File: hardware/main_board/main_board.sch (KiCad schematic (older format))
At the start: 45 parts, among them P1 USB_OTG, P2 CONN_01X02, Q1 MMBT2222, Q2 MMBT2222, SW1 SW_DPDT_x2, SW2 SW_Push, U1 ESP-12E, U2 CP2104, U3 MCP9808, U4 MMA8451Q, U5 MCP73831/2, U6 AP2112

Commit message: Separating design into main and programmer boards
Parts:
- P1: symbol USB_OTG -> USB_OTG-RESCUE-main_board
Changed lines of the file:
@@
 EESchema Schematic File Version 2
+LIBS:main_board-rescue
 LIBS:power
 LIBS:device
@@
 LIBS:zetex
 LIBS:Zilog
-LIBS:wifi_hydrometer-cache
+LIBS:main_board-cache
 EELAYER 25 0
 EELAYER END
@@
 GPIO15
 $Comp
-L USB_OTG P1
+L USB_OTG-RESCUE-main_board P1
 U 1 1 58B960C2
 P 1200 2350
@@
 	1450 4100 1350 4200
 Wire Wire Line
-	1350 4400 1350 4200
+	1350 4200 1350 4400
 Wire Wire Line
 	900  4400 1450 4400
@@
 	1450 4000 1350 3900
 Wire Wire Line
-	1350 3700 1350 3900
+	1350 3900 1350 3700
 Wire Wire Line
 	900  3700 1450 3700

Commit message: Moved components to programmer board
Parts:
- removed C1, C9: 1u, Capacitors_SMD:C_0603, symbol C
- removed P1: USB_OTG, footprint:10118192, symbol USB_OTG-RESCUE-main_board
- removed Q1, Q2: MMBT2222, TO_SOT_Packages_SMD:SOT-23, symbol Q_NPN_BEC
- removed R10, R11, R18, R19, R20, R7: 10k, Resistors_SMD:R_0603, symbol R
- removed U2: CP2104, Housings_DFN_QFN:QFN-24-1EP_4x4mm_Pitch0.5mm, symbol CP2104
- added J?: Conn_01x06, symbol Conn_01x06
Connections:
- net labels added: PROG_RXD, PROG_TXD
- net labels removed: DTR, RTS, RXD, TXD, USB_D+, USB_D-
- wire segments 148 -> 107
- no-connect marks 14 -> 10
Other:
- note added: "5V\nDETECT"
- note removed: "USB\nDETECT"
- moved on the sheet: C5, C6, C7, C8, D1, D3, D4, P2, R12, R13, SW1A, SW1B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

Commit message: Working on schematic
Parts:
- removed D4: MBR120, footprint:SOD-123FL, symbol D_Schottky
- removed J?: Conn_01x06, symbol Conn_01x06
- removed R1: 1k, Resistors_SMD:R_0603, symbol R_Small
- removed R2, R3: 10k, Resistors_SMD:R_0603, symbol R
- removed R6: 4.7k, Resistors_SMD:R_0603, symbol R
- removed SW2: SW_Push, footprint:KMR7, symbol SW_Push
- removed U1: ESP-12E, footprint:ESP-12E, symbol ESP-12E
- added C?: 1u, Capacitors_SMD:C_0603, symbol C
- added J?: eConn_02x03_Odd_Even, symbol Conn_02x03_Odd_Even
- added Q?: DMG3415U, TO_SOT_Packages_SMD:SOT-23, symbol Q_PMOS_GSD
- added R?: 100k, Resistors_SMD:R_0603, symbol R
- added U?: ESP-WROOM-32D, symbol ESP-WROOM-32D
- D1: value LED -> YLW
- D2: value LED -> RED
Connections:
- net labels added: 5V_SENSE, BAT_SENSE, LED, SCL, SDA
- net labels removed: ADC, CH_PD, GPIO12/MISO, GPIO13/MOSI, GPIO14/SCK, GPIO15, GPIO16, GPIO2, GPIO4/SDA, GPIO5/SCL
- wire segments 107 -> 98
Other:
- note removed: "5V\nDETECT"
- note removed: "BAT\nSENSE"
- moved on the sheet: C2, C3, C4, C5, C6, C7, C8, D1, D2, D3, P2, R12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

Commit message: Working on layout
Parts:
- removed C?: 1u, Capacitors_SMD:C_0603, symbol C
- removed R9: 47k, Resistors_SMD:R_0603, symbol R
- added C5, C9: 0.1u, Capacitors_SMD:C_0603, symbol C
- added C8: 10u, Capacitors_SMD:C_0805, symbol C
- added R7: 10k, Resistors_SMD:R_0603, symbol R
- D1: value YLW -> ORG
- J1: renamed from J?; footprint (none) -> Socket_Strips:Socket_Strip_Angled_2x03_Pitch2.54mm
- R8: value 24k -> 15k; Part 311-24.0KHRCT-ND -> 311-15.0KHRCT-ND
- U4: renamed from U?; footprint (none) -> footprint:ESP32-WROOM; Source (none) -> DigiKey
- gave numbers to parts that had none: 2
- renumbered C6 to C1, C2 to C10, C5 to C2, C7 to C3, C8 to C4, C3 to C6, C4 to C7, D3 to D2, D2 to D3, P2 to P1, R5 to R10, R14 to R11, R13 to R2, R16 to R3, R15 to R4, R17 to R5, R12 to R6, R4 to R9, U5 to U1, U6 to U2, U4 to U5
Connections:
- wire segments 98 -> 108
- no-connect marks 10 -> 21
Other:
- note added: "STRAPPING PINS:\nIO0\nIO2\nIO5\nIO12\nIO15"
- moved on the sheet: C10, R11

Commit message: Working on component placement
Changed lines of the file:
@@
 Connection ~ 8700 4700
-Wire Wire Line
-	1650 3900 1650 4100
 Wire Wire Line
 	3200 6650 3200 6000
@@
 NoConn ~ 6950 2400
 NoConn ~ 6950 2500
+Wire Wire Line
+	1650 3950 1650 4100
 $EndSCHEMATC

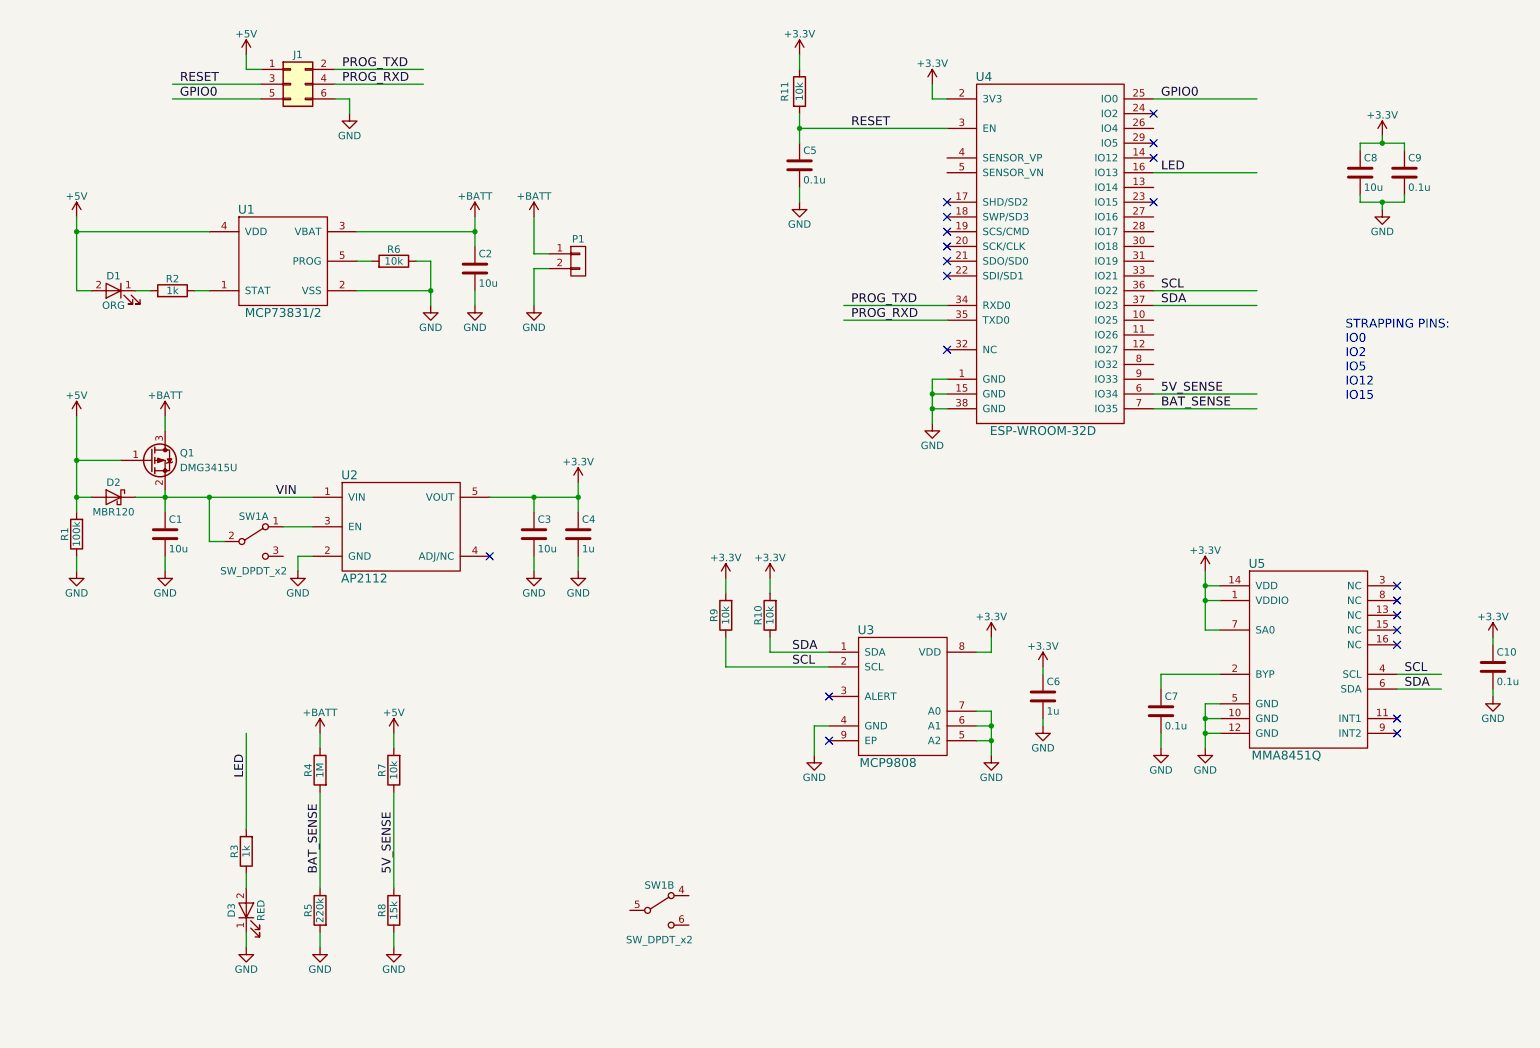
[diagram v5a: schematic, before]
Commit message: Added UV sensor.  Working on layout
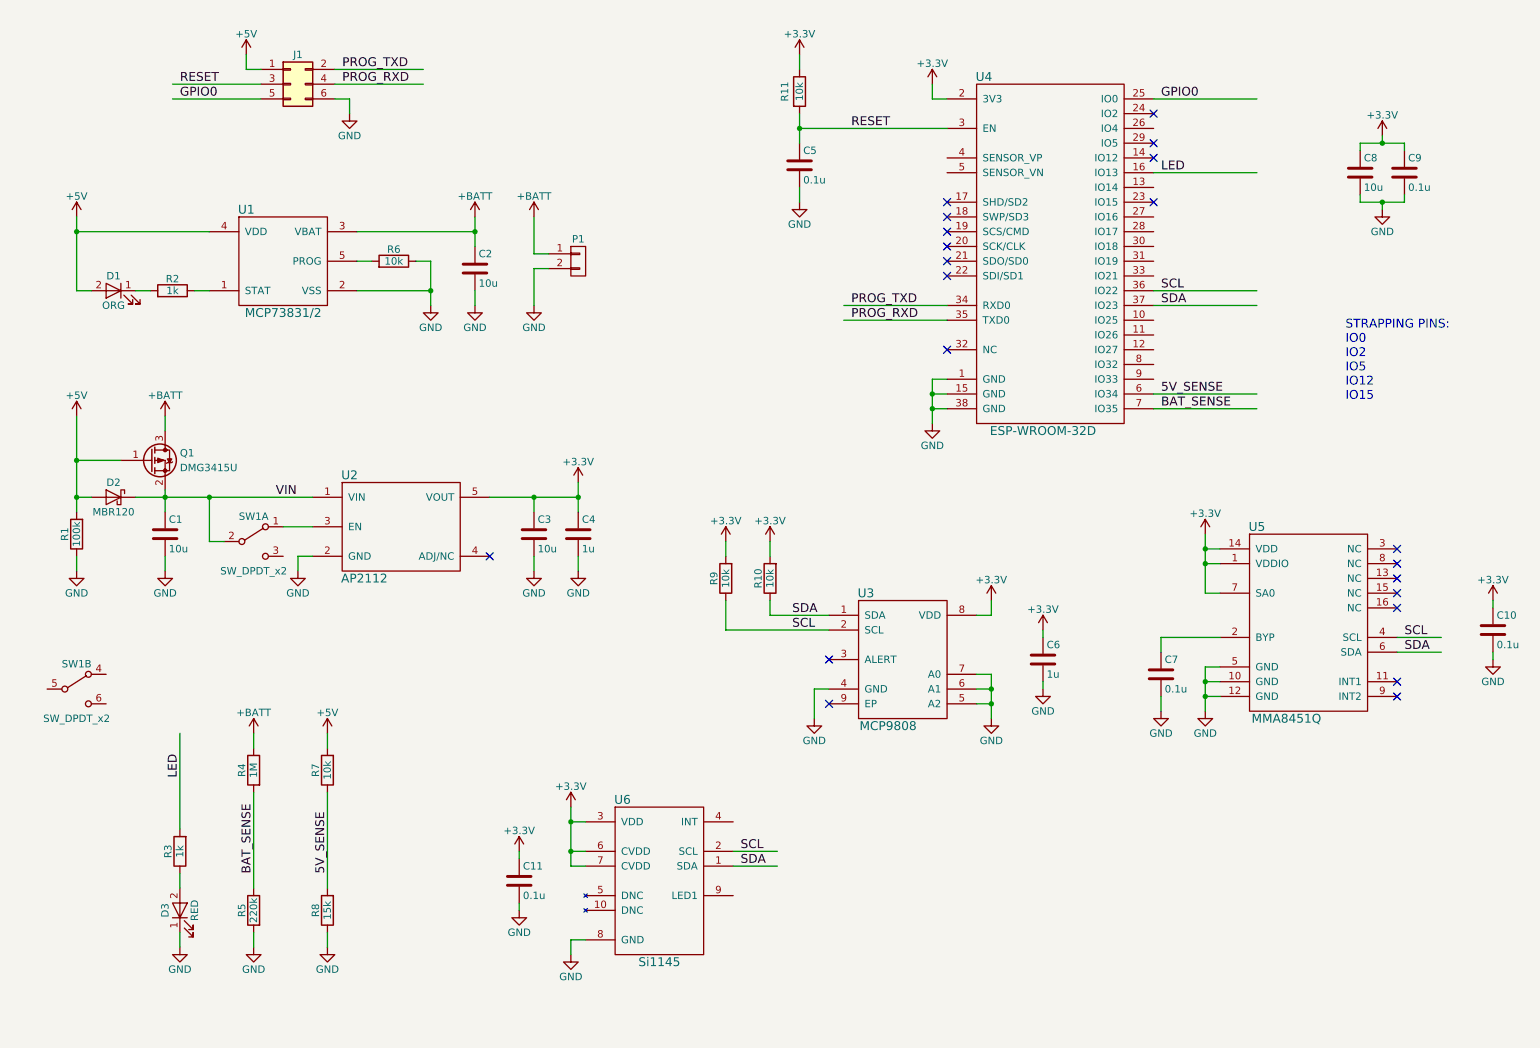
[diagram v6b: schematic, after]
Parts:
- added C11: 0.1u, Capacitors_SMD:C_0603, symbol C
- added U6: Si1145, footprint:Si1145, symbol Si1145
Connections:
- wire segments 108 -> 118
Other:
- moved on the sheet: C10, C6, C7, D3, R10, R3, R4, R5, R7, R8, R9, SW1B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

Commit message: Working on layout
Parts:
- removed C8: 10u, Capacitors_SMD:C_0805, symbol C
- removed C9: 0.1u, Capacitors_SMD:C_0603, symbol C
- renumbered C11 to C3, C3 to C4, C4 to C5, C5 to C6, C6 to C7, C7 to C8, C10 to C9, R7 to R6, R8 to R7, R6 to R8, U6 to U3, U3 to U4, U4 to U5, U5 to U6
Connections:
- wire segments 118 -> 110
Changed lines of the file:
@@
 $EndComp
 $Comp
-L R R6
+L R R8
 U 1 1 58B92660
 P 3200 2400
-F 0 "R6" V 3280 2400 50  0000 C CNN
+F 0 "R8" V 3280 2400 50  0000 C CNN
 F 1 "10k" V 3200 2400 50  0000 C CNN
 F 2 "Resistors_SMD:R_0603" V 3130 2400 50  0001 C CNN
@@
 $EndComp
 $Comp
-L C C3
+L C C4
 U 1 1 58B97FCA
 P 4150 4250
-F 0 "C3" H 4175 4350 50  0000 L CNN
+F 0 "C4" H 4175 4350 50  0000 L CNN
 F 1 "10u" H 4175 4150 50  0000 L CNN
 F 2 "Capacitors_SMD:C_0805" H 4188 4100 50  0001 C CNN
@@
 $EndComp
 $Comp
-L C C4
+L C C5
 U 1 1 58B98035
 P 4450 4250
-F 0 "C4" H 4475 4350 50  0000 L CNN
+F 0 "C5" H 4475 4350 50  0000 L CNN
 F 1 "1u" H 4475 4150 50  0000 L CNN
 F 2 "Capacitors_SMD:C_0603" H 4488 4100 50  0001 C CNN
@@
 $EndComp
 $Comp
-L MCP9808 U3
+L MCP9808 U4
 U 1 1 58BACCE5
 P 6650 5100
-F 0 "U3" H 6400 5550 60  0000 C CNN
+F 0 "U4" H 6400 5550 60  0000 C CNN
 F 1 "MCP9808" H 6550 4650 60  0000 C CNN
 F 2 "Housings_DFN_QFN:DFN-8-1EP_3x2mm_Pitch0.5mm" H 6650 5100 60  0001 C CNN
@@
 $EndComp
 $Comp
-L MMA8451Q U5
+L MMA8451Q U6
 U 1 1 58BAE024
 P 9400 4700
-F 0 "U5" H 9050 5200 60  0000 C CNN
+F 0 "U6" H 9050 5200 60  0000 C CNN
 F 1 "MMA8451Q" H 9250 3900 60  0000 C CNN
 F 2 "footprint:MMA8451Q" H 9400 4700 60  0001 C CNN
@@
 $EndComp
 $Comp
-L C C10
+L C C9
 U 1 1 58BAF20C
 P 10650 4900
-F 0 "C10" H 10675 5000 50  0000 L CNN
+F 0 "C9" H 10675 5000 50  0000 L CNN
 F 1 "0.1u" H 10675 4800 50  0000 L CNN
 F 2 "Capacitors_SMD:C_0603" H 10688 4750 50  0001 C CNN
@@
 $EndComp
 $Comp
-L C C7
+L C C8
 U 1 1 58BB0721
 P 8400 5200
-F 0 "C7" H 8425 5300 50  0000 L CNN
+F 0 "C8" H 8425 5300 50  0000 L CNN
 F 1 "0.1u" H 8425 5100 50  0000 L CNN
 F 2 "Capacitors_SMD:C_0603" H 8438 5050 50  0001 C CNN
@@
 NoConn ~ 10000 5350
 $Comp
-L +3.3V #PWR42
+L +3.3V #PWR40
 U 1 1 58BB1307
 P 10650 4700
-F 0 "#PWR42" H 10650 4550 50  0001 C CNN
+F 0 "#PWR40" H 10650 4550 50  0001 C CNN
 F 1 "+3.3V" H 10650 4840 50  0000 C CNN
 F 2 "" H 10650 4700 50  0000 C CNN
@@
 $EndComp
 $Comp
-L GND #PWR43
+L GND #PWR41
 U 1 1 58BB1E75
 P 10650 5100
-F 0 "#PWR43" H 10650 4850 50  0001 C CNN
+F 0 "#PWR41" H 10650 4850 50  0001 C CNN
 F 1 "GND" H 10650 4950 50  0000 C CNN
 F 2 "" H 10650 5100 50  0000 C CNN
@@
 $EndComp
 $Comp
-L C C6
+L C C7
 U 1 1 58BB5C80
 P 7600 5100
-F 0 "C6" H 7625 5200 50  0000 L CNN
+F 0 "C7" H 7625 5200 50  0000 L CNN
 F 1 "1u" H 7625 5000 50  0000 L CNN
 F 2 "Capacitors_SMD:C_0603" H 7638 4950 50  0001 C CNN
@@
 $EndComp
 $Comp
-L ESP-WROOM-32D U4
+L ESP-WROOM-32D U5
 U 1 1 5A484B62
 P 7650 2350
-F 0 "U4" H 7200 3550 60  0000 C CNN
+F 0 "U5" H 7200 3550 60  0000 C CNN
 F 1 "ESP-WROOM-32D" H 7600 1150 60  0000 C CNN
 F 2 "footprint:ESP32-WROOM" H 6500 3100 60  0001 C CNN
@@
 NoConn ~ 8350 1700
 $Comp
-L R R7
+L R R6
 U 1 1 5A47FE47
 P 2750 5850
-F 0 "R7" V 2830 5850 50  0000 C CNN
+F 0 "R6" V 2830 5850 50  0000 C CNN
 F 1 "10k" V 2750 5850 50  0000 C CNN
 F 2 "Resistors_SMD:R_0603" V 2680 5850 50  0001 C CNN
@@
 $EndComp
 $Comp
-L R R8
+L R R7
 U 1 1 5A47FED2
 P 2750 6800
-F 0 "R8" V 2830 6800 50  0000 C CNN
+F 0 "R7" V 2830 6800 50  0000 C CNN
 F 1 "15k" V 2750 6800 50  0000 C CNN
 F 2 "Resistors_SMD:R_0603" V 2680 6800 50  0001 C CNN
@@
 $EndComp
 $Comp
-L C C9
-U 1 1 5A48A3BF
-P 10050 1800
-F 0 "C9" H 10075 1900 50  0000 L CNN
-F 1 "0.1u" H 10075 1700 50  0000 L CNN
-F 2 "Capacitors_SMD:C_0603" H 10088 1650 50  0001 C CNN
-F 3 "" H 10050 1800 50  0000 C CNN
-F 4 "DigiKey" H 10050 1800 60  0001 C CNN "Source"
-F 5 "311-1344-1-ND" H 10050 1800 60  0001 C CNN "Part"
-	1    10050 1800
-	1    0    0    -1
-$EndComp
-$Comp
-L +3.3V #PWR40
-U 1 1 5A48A902
-P 9900 1550
-F 0 "#PWR40" H 9900 1400 50  0001 C CNN
-F 1 "+3.3V" H 9900 1690 50  0000 C CNN
-F 2 "" H 9900 1550 50  0000 C CNN
-F 3 "" H 9900 1550 50  0000 C CNN
-	1    9900 1550
-	1    0    0    -1
-$EndComp
-$Comp
-L GND #PWR41
-U 1 1 5A48A970
-P 9900 2050
-F 0 "#PWR41" H 9900 1800 50  0001 C CNN
-F 1 "GND" H 9900 1900 50  0000 C CNN
-F 2 "" H 9900 2050 50  0000 C CNN
-F 3 "" H 9900 2050 50  0000 C CNN
-	1    9900 2050
-	1    0    0    -1
-$EndComp
-$Comp
-L C C8
-U 1 1 5A48ACF8
-P 9750 1800
-F 0 "C8" H 9775 1900 50  0000 L CNN
-F 1 "10u" H 9775 1700 50  0000 L CNN
-F 2 "Capacitors_SMD:C_0805" H 9788 1650 50  0001 C CNN
-F 3 "" H 9750 1800 50  0000 C CNN
-F 4 "DigiKey" H 9750 1800 60  0001 C CNN "Source"
-F 5 "311-1460-1-ND" H 9750 1800 60  0001 C CNN "Part"
-	1    9750 1800
-	1    0    0    -1
-$EndComp
-Wire Wire Line
-	9750 1950 9750 2000
-Wire Wire Line
-	9750 2000 10050 2000
-Wire Wire Line
-	10050 2000 10050 1950
-Wire Wire Line
-	9900 2050 9900 2000
-Connection ~ 9900 2000
-Wire Wire Line
-	9750 1650 9750 1600
-Wire Wire Line
-	9750 1600 10050 1600
-Wire Wire Line
-	10050 1600 10050 1650
-Wire Wire Line
-	9900 1550 9900 1600
-Connection ~ 9900 1600
-$Comp
-L C C5
+L C C6
 U 1 1 5A48B9D9
 P 5950 1750
-F 0 "C5" H 5975 1850 50  0000 L CNN
+F 0 "C6" H 5975 1850 50  0000 L CNN
 F 1 "0.1u" H 5975 1650 50  0000 L CNN
 F 2 "Capacitors_SMD:C_0603" H 5988 1600 50  0001 C CNN
@@
 NoConn ~ 8350 1600
 NoConn ~ 8350 2000
-Text Notes 9650 3350 0    60   ~ 0
+Text Notes 9800 1750 0    60   ~ 0
 STRAPPING PINS:\nIO0\nIO2\nIO5\nIO12\nIO15
 NoConn ~ 6950 2000
@@
 	1650 3950 1650 4100
 $Comp
-L Si1145 U6
+L Si1145 U3
 U 1 1 5A598AD2
 P 5000 6600
-F 0 "U6" H 4750 7150 60  0000 C CNN
+F 0 "U3" H 4750 7150 60  0000 C CNN
 F 1 "Si1145" H 5000 6050 60  0000 C CNN
 F 2 "footprint:Si1145" H 4950 6600 60  0001 C CNN
@@
 SCL
 $Comp
-L C C11
+L C C3
 U 1 1 5A59A2EC
 P 4050 6600
-F 0 "C11" H 4075 6700 50  0000 L CNN
+F 0 "C3" H 4075 6700 50  0000 L CNN
 F 1 "0.1u" H 4075 6500 50  0000 L CNN
 F 2 "Capacitors_SMD:C_0603" H 4088 6450 50  0001 C CNN

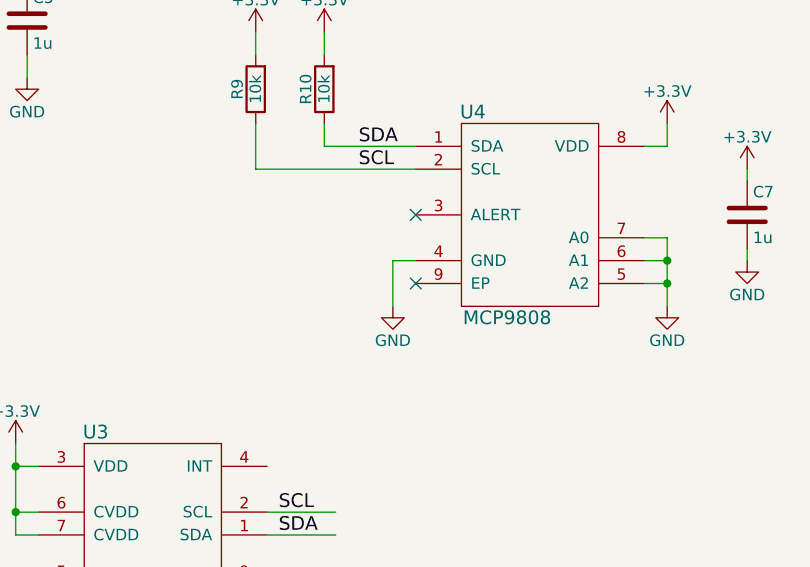
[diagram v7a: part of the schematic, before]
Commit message: Finished routing board
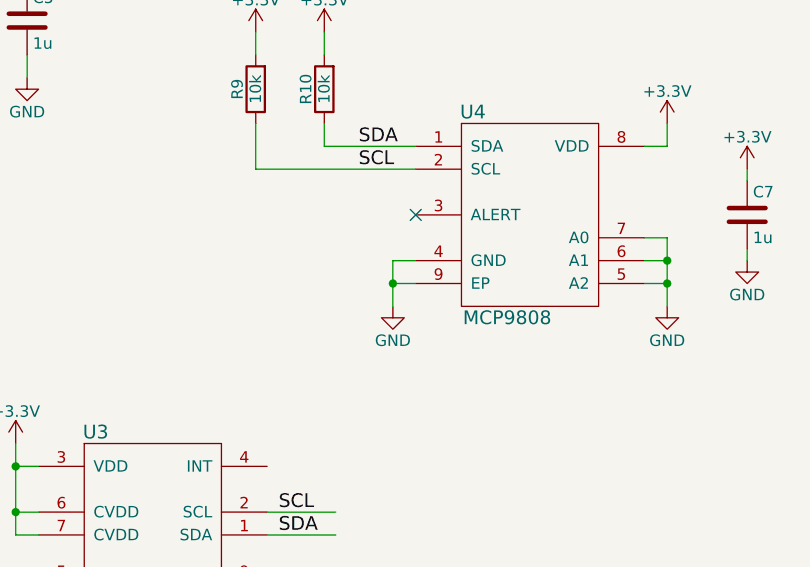
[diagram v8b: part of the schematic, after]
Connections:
- wire segments 110 -> 111
- no-connect marks 21 -> 20
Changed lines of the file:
@@
 Text Label 2400 4000 0    60   ~ 0
 VIN
-NoConn ~ 6150 5400
 $Comp
 L +5V #PWR7
@@
 Wire Wire Line
 	5800 6500 5500 6500
+Wire Wire Line
+	6150 5400 6050 5400
+Connection ~ 6050 5400
 $EndSCHEMATC
